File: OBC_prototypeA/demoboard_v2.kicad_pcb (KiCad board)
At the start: 2 copper layers, 95.9 x 90.2 mm, 130 parts, among them J1 PC104-8BIT, P1 3v3_IN_CONNECTOR, P10 FLASH_CS, P11 USB_5V, P12 JTAG_20PIN, P13 WD_EN, P2 INA_INPUT, P3 INA_GND, P4 INA_EN, P5 INA_OUTPUT, P6 USB_PORT, P7 OSC_FUALT_INJECT, P8 RTC_SPI, P9 FLASH_SPI, Q1 DMN2075U, Q2 DMN2075U, Q3 1v2_GOOD, Q4 DMN2075U, Q5 DMN2075U, SW1 SPST, SW2 SPST, U1 TMS570LS0714, U10 FT230XQ-R, U2 AP7331, U3 AP7361_3.3v, U4 INA301, U5 FLASH_IS25LP016D, U6 FLASH_IS25LP016D, U7 FLASH_IS25LP016D, U8 AB-RTCMC-EOA9-S3, U9 TPS3110, Y1 XTAL

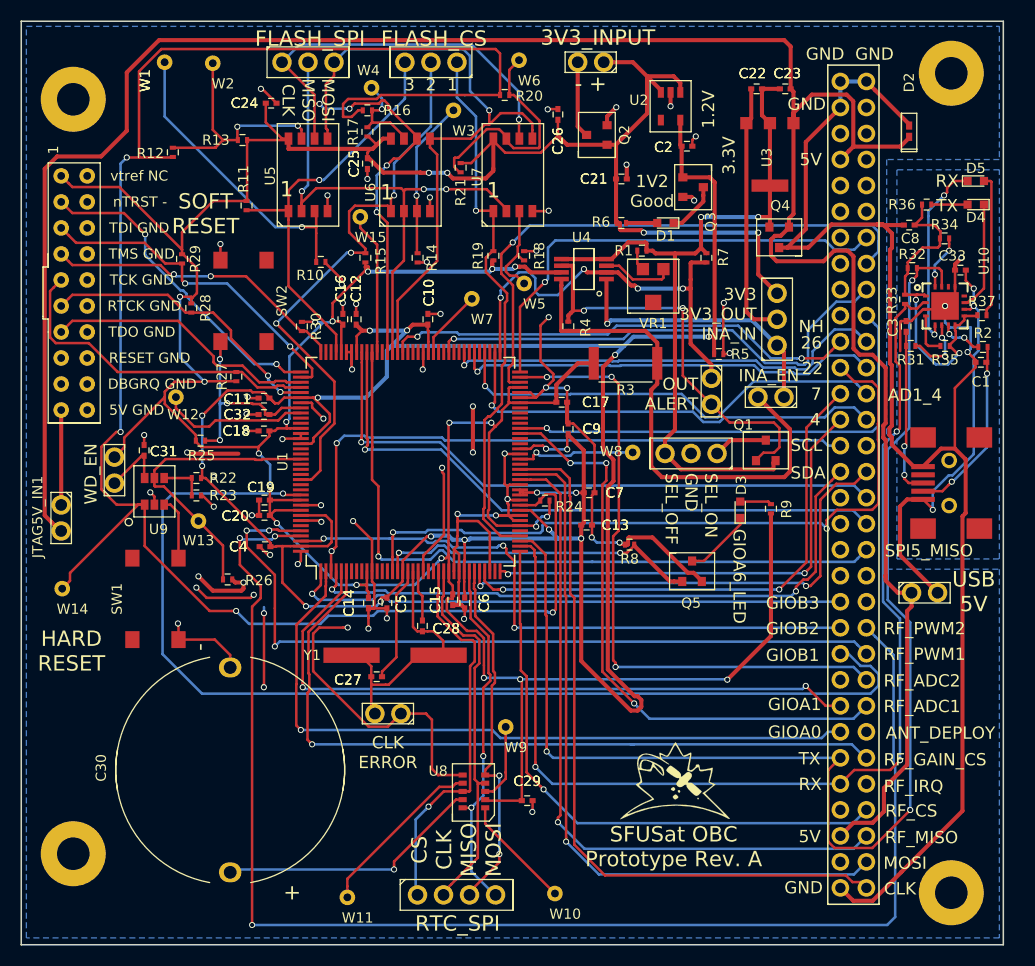
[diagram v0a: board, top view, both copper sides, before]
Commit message: Added gerbers, redid USB section (just need to add differential pair), fixed USB connector paste
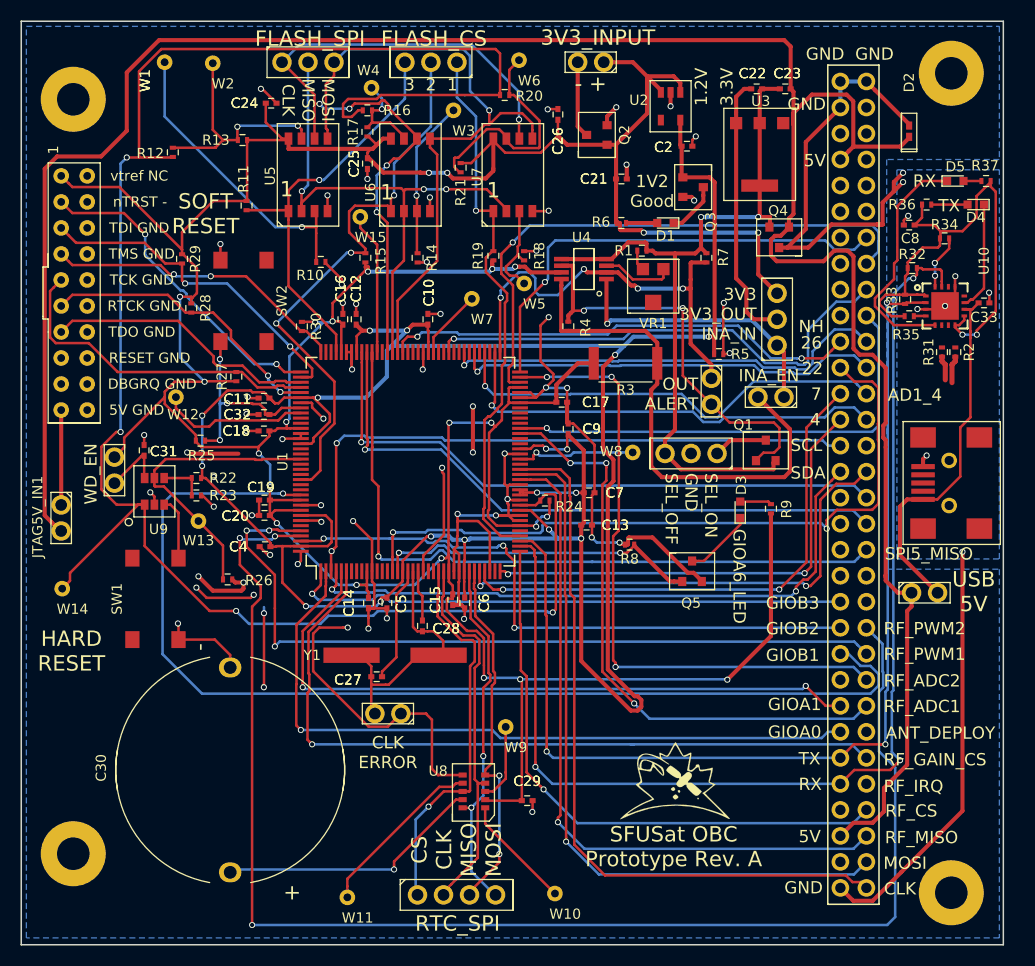
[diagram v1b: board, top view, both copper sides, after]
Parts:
- removed C1, C3: 47pF, SFUSat:C_0402
- moved R37 13.1 mm to (194.2, 35.6), turned to 180 degrees
- moved R35 4.55 mm to (186.7, 48.8), turned to 0 degrees
- moved C33 3.94 mm to (194.0, 47.5), turned to 0 degrees
- moved R31 3.11 mm to (189.9, 52.3), turned to 270 degrees
- moved R2 2.75 mm to (191.2, 52.3), turned to 270 degrees
- moved D5 2.00 mm to (191.2, 35.6)
- moved U3 1.00 mm to (172.1, 33.0)
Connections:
- net Net-(R2-Pad1) renamed /PC104_Connector/RUSB_N
- net Net-(R31-Pad1) renamed /PC104_Connector/RUSB_P
- net USB_2 renamed USB_N
- net USB_3 renamed USB_P
- R32 pad 2: UART_TX -> UART_RX
- R33 pad 2: UART_RX -> UART_TX
- U10 pad 15: UART_TX -> UART_RX
- U10 pad 2: UART_RX -> UART_TX
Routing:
- net 104_In_GND: track 154.0 -> 97.5 mm, vias 3 -> 9
- net UART_TX: track 129.1 -> 103.7 mm
- net FTDI_VCCIO: track 32.5 -> 50.0 mm
- net USB_N: track 17.9 -> 2.67 mm, vias 2 -> 0
- net USB_P: track 16.4 -> 2.40 mm, vias 2 -> 0
- net Net-(D5-Pad2): track 14.0 -> 1.75 mm
- net /PC104_Connector/RUSB_P: track 6.47 -> 0.04 mm, vias 2 -> 0
- net USB_5V: track 41.0 -> 35.8 mm, vias 3 -> 0
- net UART_RX: track 108.9 -> 114.0 mm
- net Net-(D5-Pad1): track 18.5 -> 23.3 mm, vias 2 -> 0
- net /PC104_Connector/RUSB_N: track 4.26 -> 0.00 mm, vias 2 -> 0
- net Net-(R35-Pad2): track 4.22 -> 1.19 mm
- net 3v3_OUTPUT: track 25.3 -> 26.5 mm
- net Net-(R34-Pad2): track 5.31 -> 5.87 mm
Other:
- net class USB added: clearance 0.1524, trace_width 0.5, via_dia 0.6, via_drill 0.4

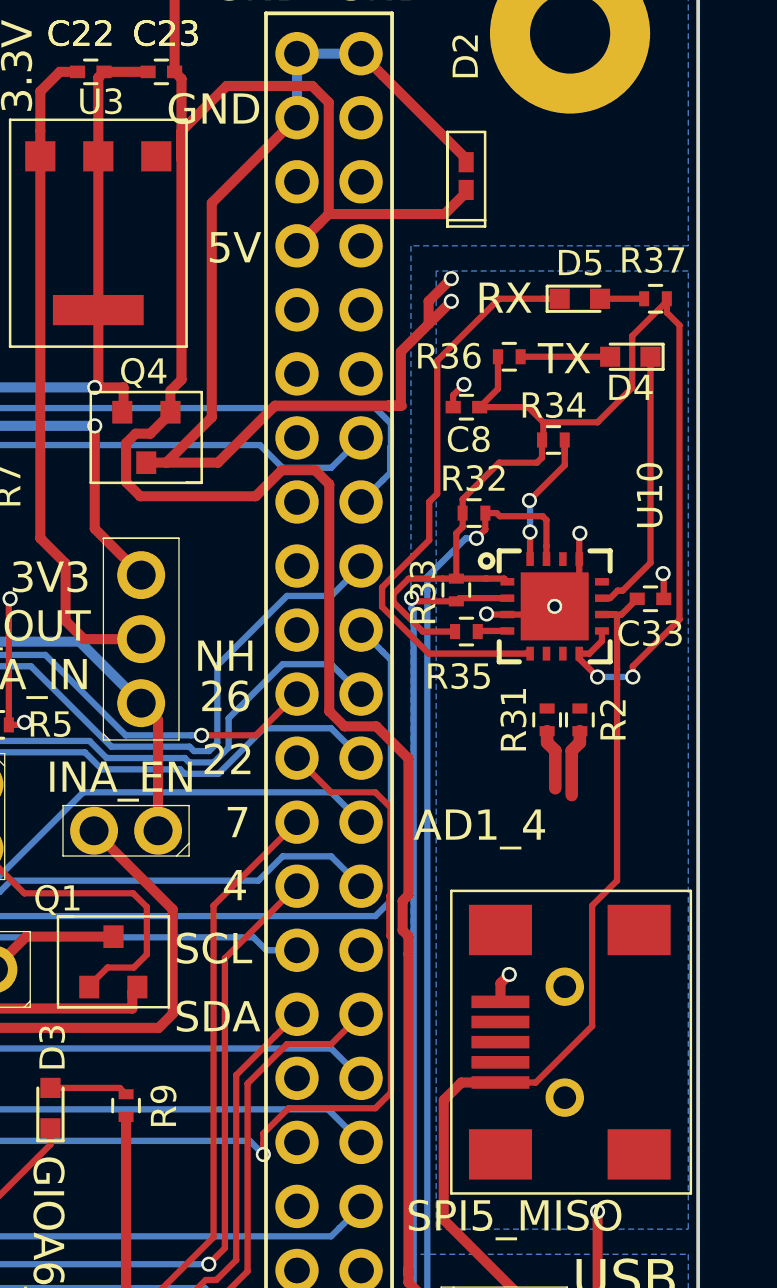
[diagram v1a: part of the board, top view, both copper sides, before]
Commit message: Length mached USB traces and cleaned up FTDI region
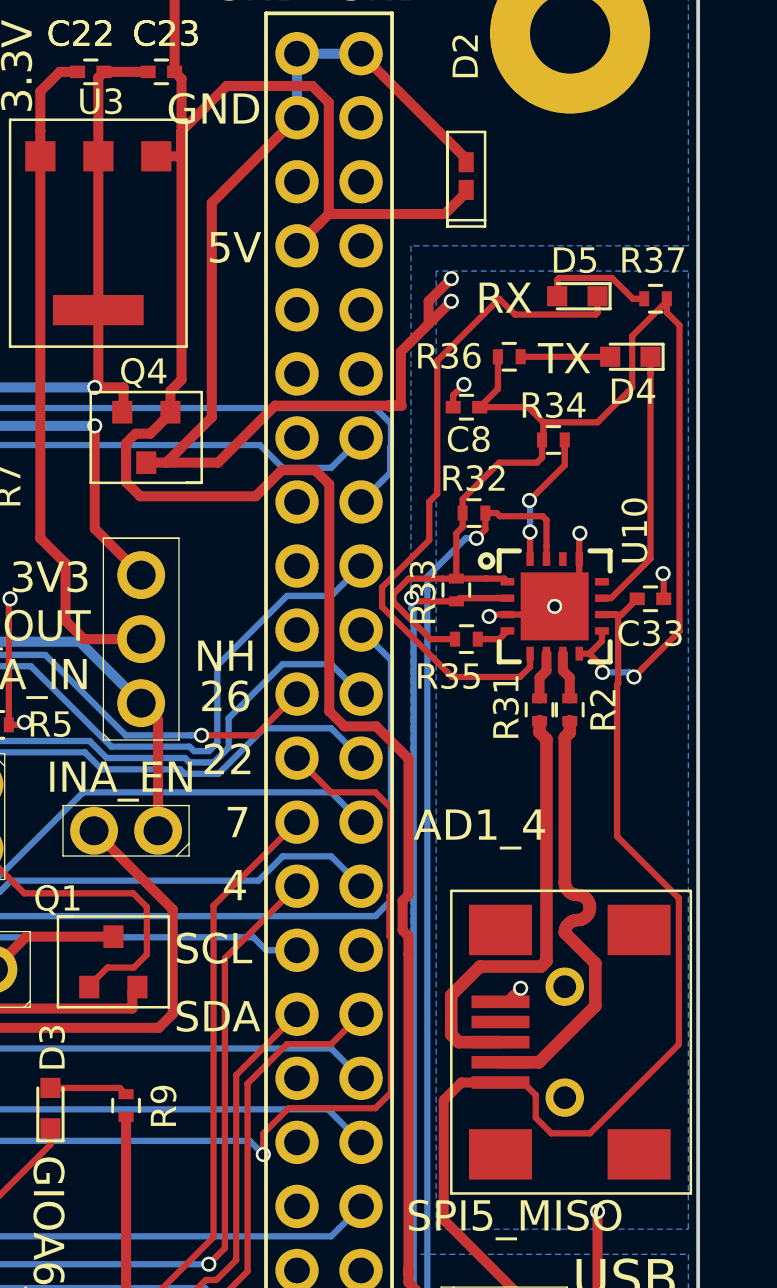
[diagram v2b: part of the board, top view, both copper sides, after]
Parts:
- moved R2 0.57 mm to (190.8, 51.9)
- moved R31 0.50 mm to (189.6, 51.9)
- moved R35 0.30 mm to (186.7, 49.1)
- moved D5 0.14 mm to (191.1, 35.5), turned to 180 degrees
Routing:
- net USB_P: track 2.40 -> 17.6 mm
- net USB_N: track 2.67 -> 17.7 mm
- net USB_5V: track 35.8 -> 42.5 mm
- net Net-(D5-Pad1): track 23.3 -> 26.7 mm
- net Net-(D5-Pad2): track 1.75 -> 4.47 mm
- net /PC104_Connector/RUSB_P: track 0.04 -> 1.92 mm
- net /PC104_Connector/RUSB_N: track 0.00 -> 1.89 mm
- net 5v0: track 233.4 -> 234.4 mm

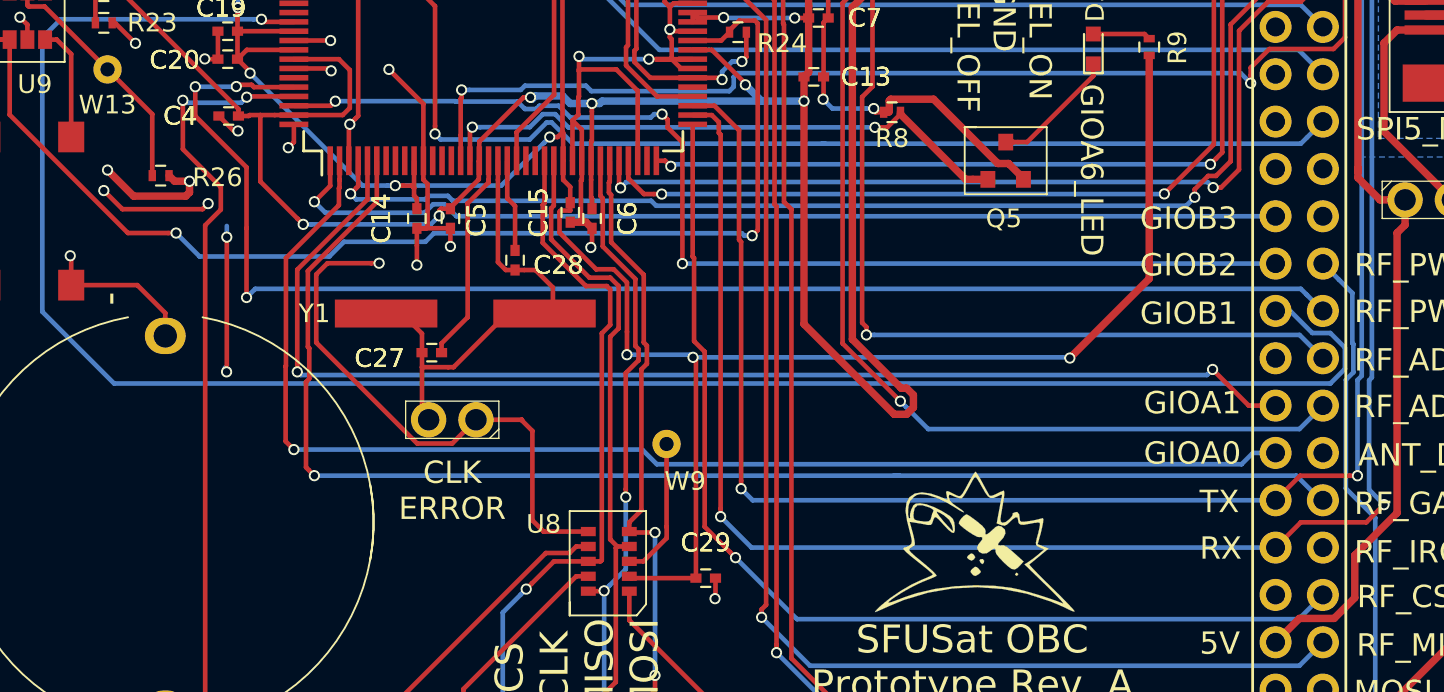
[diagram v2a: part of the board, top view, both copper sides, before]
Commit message: Fixed oscillator circuit.
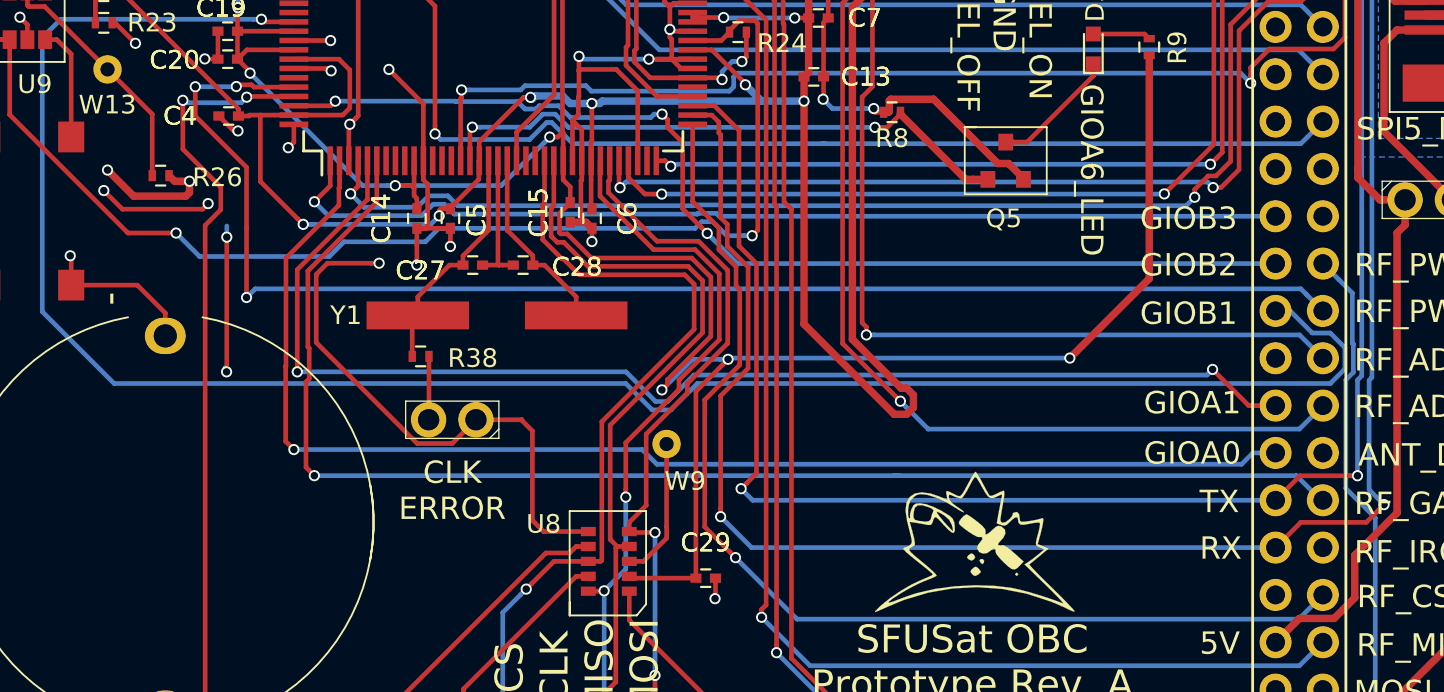
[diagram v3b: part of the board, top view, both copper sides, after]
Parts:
- added R38: 1k, SFUSat:R_0402, F.Cu at (134.1, 84.2)
- moved C27 5.19 mm to (136.9, 79.3)
- moved Y1 1.70 mm to (138.2, 82.0)
- moved C28 0.50 mm to (139.6, 79.3), turned to 0 degrees
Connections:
- C28 pad 1: Net-(C27-Pad1) -> Net-(C27-Pad2)
- P7 pad 2: Net-(C27-Pad1) -> Net-(P7-Pad2)
- U1 pad 18: Net-(C27-Pad2) -> Net-(C27-Pad1)
- U1 pad 19: Net-(C27-Pad1) -> Net-(C27-Pad2)
- Y1 pad 2: Net-(C27-Pad1) -> Net-(C28-Pad2)
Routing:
- net Net-(C27-Pad1): track 24.7 -> 12.6 mm
- net 3v3: track 396.9 -> 403.5 mm
- net RTC_CLK: track 36.2 -> 42.6 mm
- net RTC_CS: track 37.5 -> 44.0 mm
- net Net-(C28-Pad2): track 4.99 -> 10.2 mm
- net RTC_MISO: track 35.4 -> 40.3 mm
- net RTC_MOSI: track 34.9 -> 39.8 mm
- net Net-(C27-Pad2): track 11.3 -> 7.27 mm
- net Net-(P7-Pad2): track 0.00 -> 3.91 mm
- net GIOB2: track 61.4 -> 59.7 mm
- net RF_CS: track 57.6 -> 59.2 mm
- net UART_RX: track 114.0 -> 115.2 mm
- net GIOA1: track 66.4 -> 67.6 mm
- net GIOB1: track 106.2 -> 107.3 mm
- net UART_TX: track 103.7 -> 104.4 mm
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
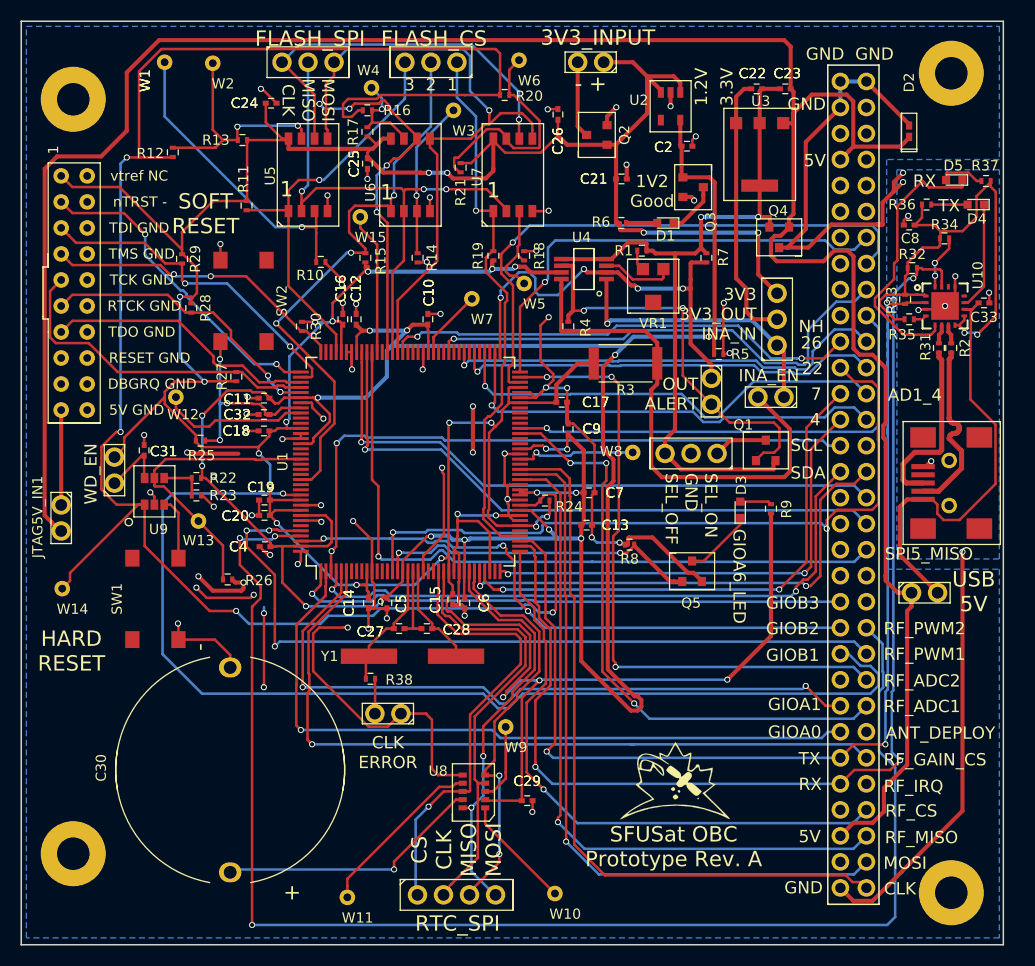
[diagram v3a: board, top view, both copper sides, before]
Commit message: Routed signal traces outside of the vicinity of the oscillator
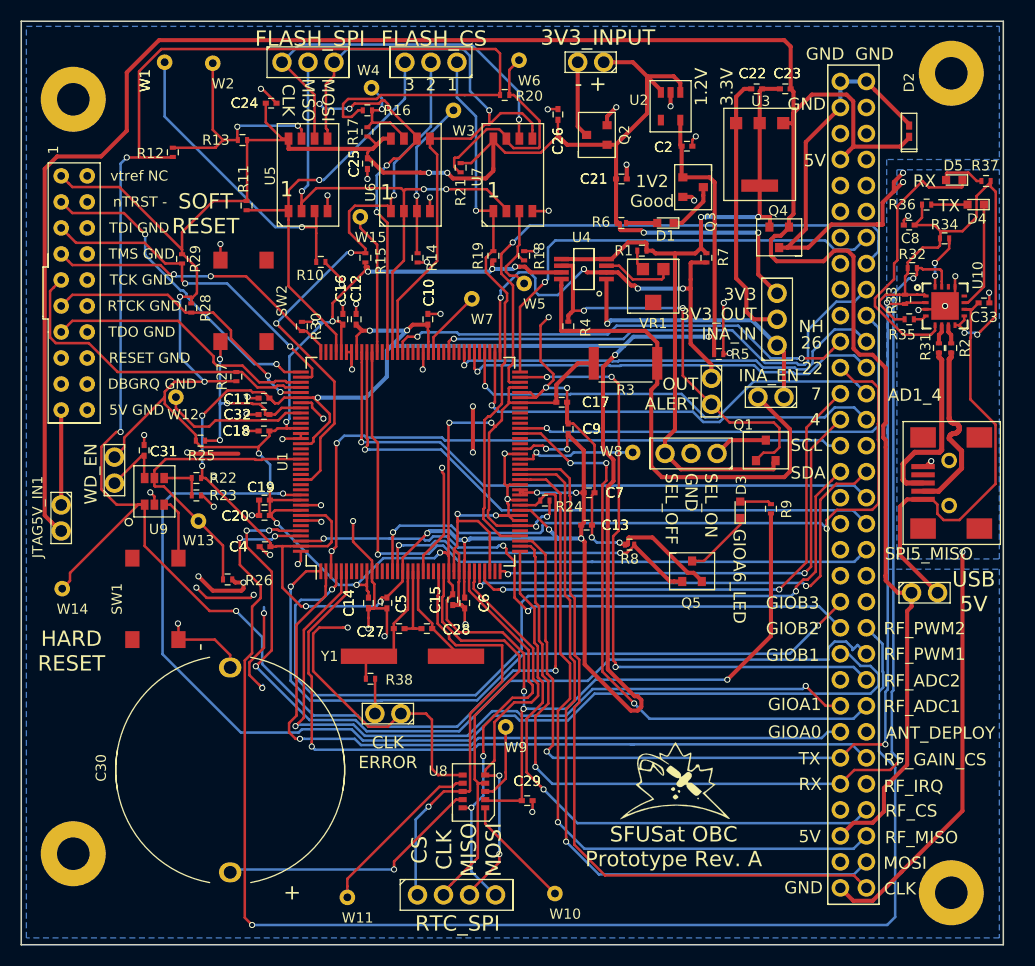
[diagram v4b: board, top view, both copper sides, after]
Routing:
- net I2C_SDA: track 62.0 -> 83.4 mm
- net GIOB3: track 55.0 -> 71.3 mm, vias 1 -> 2
- net MASTER_RESET: track 186.3 -> 199.0 mm
- net RF_PWM1: track 76.3 -> 87.9 mm
- net GIOA1: track 67.6 -> 73.9 mm
- net 3v3: track 403.5 -> 397.7 mm
- net GIOB1: track 107.3 -> 110.6 mm
- net GND: track 216.0 -> 218.7 mm
- net RTC_CS: track 44.0 -> 41.8 mm
- net GIOA0: track 70.1 -> 72.1 mm
- net RTC_CLK: track 42.6 -> 41.3 mm
- net (no net): track 24.0 -> 25.2 mm
- net GIOA6: track 31.9 -> 32.7 mm
- net RF_MISO: track 68.4 -> 69.2 mm
- net 1v2: track 262.5 -> 263.2 mm
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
